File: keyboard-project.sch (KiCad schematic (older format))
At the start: 14 parts

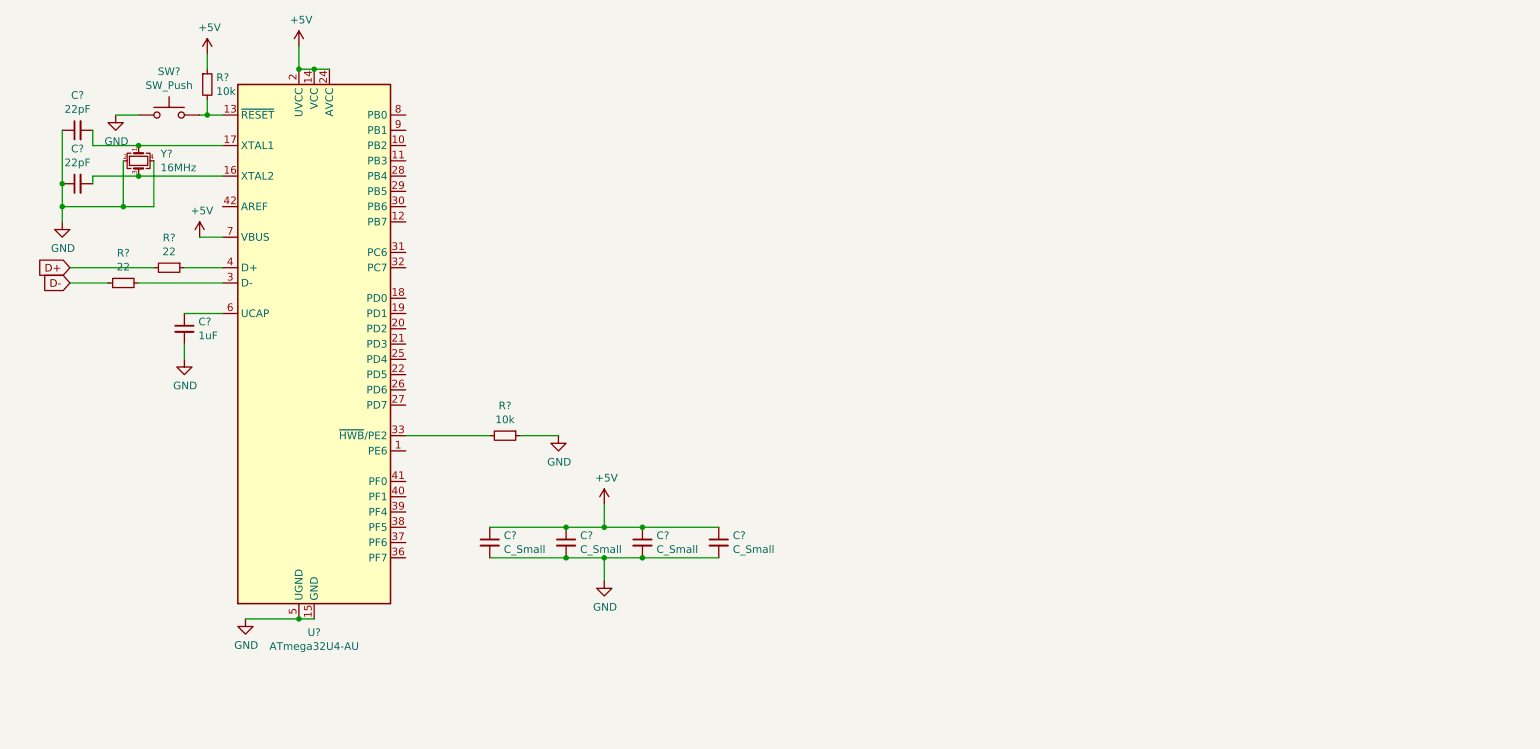
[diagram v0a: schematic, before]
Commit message: Added: Switch Matrix
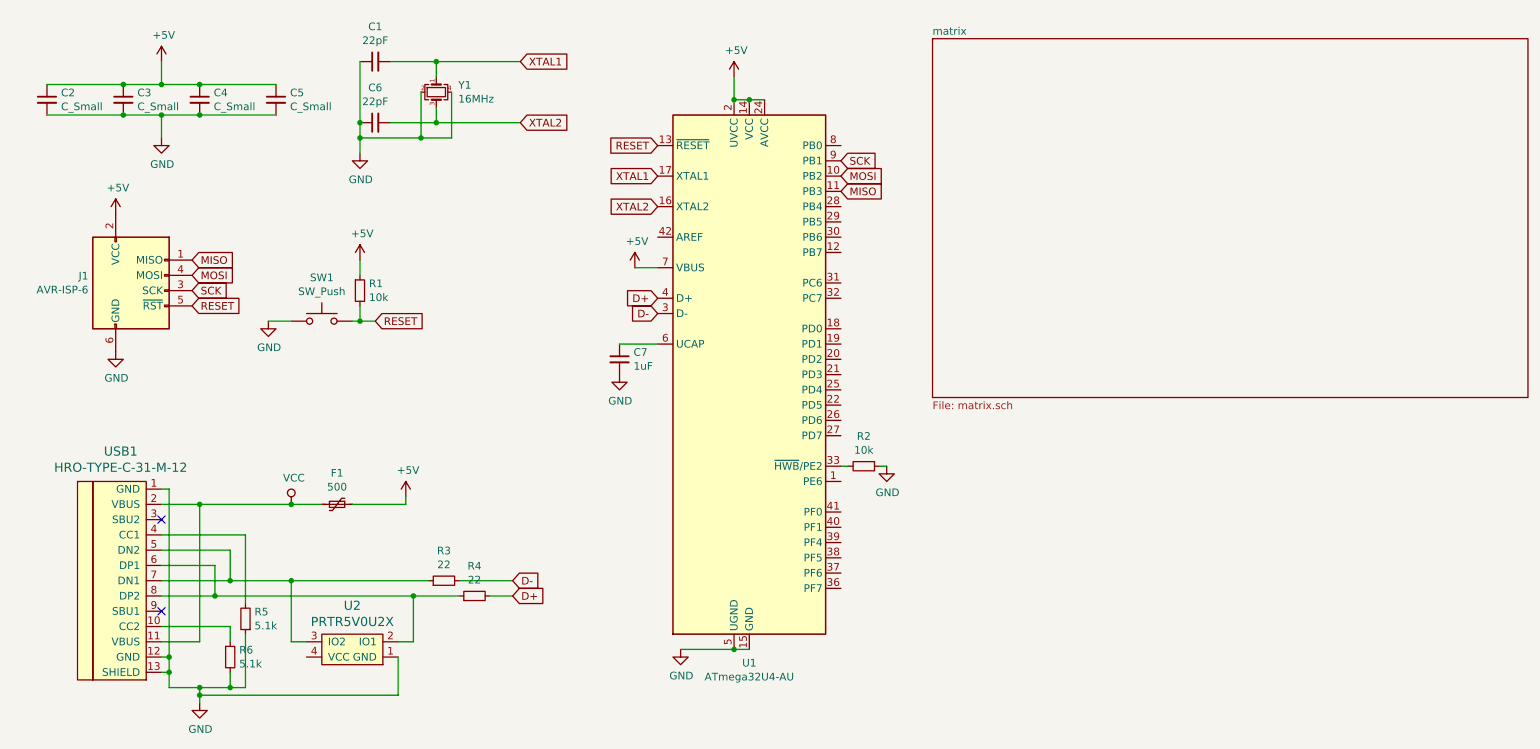
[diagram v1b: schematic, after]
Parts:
- removed R? (x2): 22, symbol Device:R_Small
- added F1: 500, symbol Device:Polyfuse_Small
- added J1: AVR-ISP-6, symbol Connector:AVR-ISP-6
- added R3, R4: 22, symbol Device:R_Small
- added R5, R6: 5.1k, symbol Device:R_Small
- added U2: PRTR5V0U2X, symbol random-keyboard-parts:PRTR5V0U2X
- added USB1: HRO-TYPE-C-31-M-12, symbol Type-C:HRO-TYPE-C-31-M-12
- gave numbers to parts that had none: 12
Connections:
- net +5V: now also F1.1, J1.2 (VCC)
- net D+: now also U1.4 (D+), R4.2
- net D-: now also U1.3 (D-), R3.2
- net GND: now also J1.6 (GND), R5.1, R6.2, U2.1 (GND), USB1.1 (GND), USB1.12 (GND), USB1.13 (SHIELD)
- net MOSI: now reaches U1.10 (PB2)
- net MOSI: now also J1.4 (MOSI)
- net MISO: now reaches U1.11 (PB3)
- net MISO: now also J1.1 (MISO)
- net RESET: now reaches R1.2, SW1.2, U1.13 (~RESET)
- net RESET: now also J1.5 (~RST)
- net XTAL2: now reaches C6.2, U1.16 (XTAL2), Y1.3
- net XTAL1: now reaches C1.2, U1.17 (XTAL1), Y1.1
- net SCK: now reaches U1.9 (PB1)
- net SCK: now also J1.3 (SCK)
- new net: R6.1, USB1.10 (CC2)
- new net: R5.2, USB1.4 (CC1)
- new net: R3.1, U2.3 (IO2), USB1.5 (DN2), USB1.7 (DN1)
- new net: R4.1, U2.2 (IO1), USB1.6 (DP1), USB1.8 (DP2)
- new net VCC: F1.2, USB1.11 (VBUS), USB1.2 (VBUS)
- no-connect marks 0 -> 2
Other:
- moved on the sheet: C1, C2, C3, C4, C5, C6, C7, R1, R2, SW1, U1, Y1
